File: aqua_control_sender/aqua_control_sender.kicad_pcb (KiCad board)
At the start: 2 copper layers, 66 x 80 mm, 37 parts, among them J1 USB_C, J4 Conn_01x03, J5 Conn_01x03, Q2 IRLML6402, SW1 RESET, SW2 BOOT, U1 ESP32-S3-WROOM-1, U2 LM1117-3.3, U3 RA-02_LORA

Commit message: routing completed
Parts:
- removed Q2: IRLML6402, Package_TO_SOT_SMD:SOT-23
- added J10: ~, Library:TP4056, F.Cu at (65.1, 59.8)
- R8: moved to B.Cu
- moved C7 96.0 mm to (33.9, 92.8), turned to -90 degrees
- moved C6 92.8 mm to (36.1, 92.8), turned to -90 degrees
- moved R17 91.1 mm to (36.1, 96.8)
- moved C5 76.1 mm to (46.1, 72.7), turned to 180 degrees
- moved C4 75.3 mm to (46.1, 74.9), turned to 180 degrees
- moved C9 74.8 mm to (40.4, 62.3), turned to 180 degrees
- moved J8 74.2 mm to (80.7, 92.8)
- moved C8 74.0 mm to (40.4, 65.0), turned to 180 degrees
- moved D4 63.2 mm to (65.2, 50.4), turned to 180 degrees
- moved D3 61.5 mm to (65.2, 53.0), turned to 180 degrees
- moved SW2 53.8 mm to (60.6, 33.4), turned to 180 degrees
- moved R5 51.7 mm to (47.1, 63.2), turned to -90 degrees
- moved TP3 44.3 mm to (60.8, 105.0), turned to 0 degrees
- moved J5 43.8 mm to (41.2, 27.1)
- moved R8 43.2 mm to (60.7, 56.2), turned to 180 degrees
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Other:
- board size 66 x 80 mm -> 54 x 86 mm

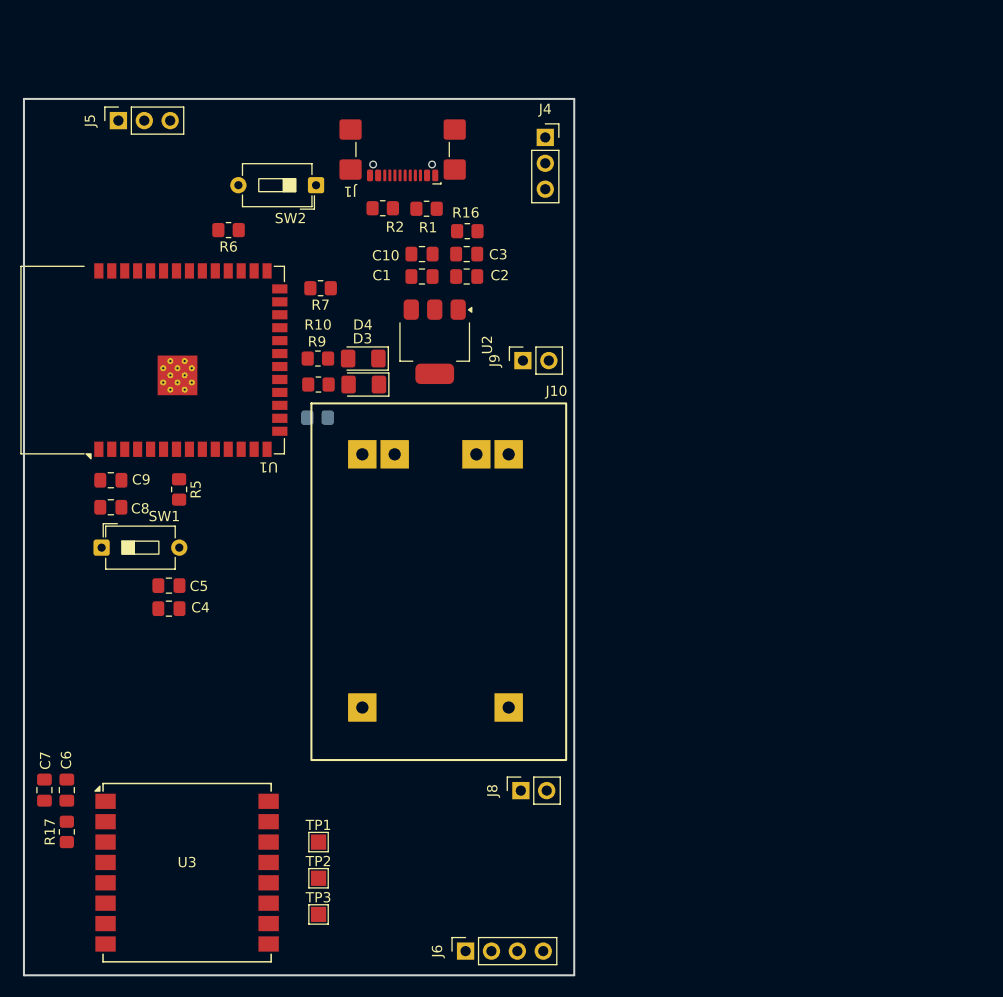
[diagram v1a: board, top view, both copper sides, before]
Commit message: completed routing and added logo
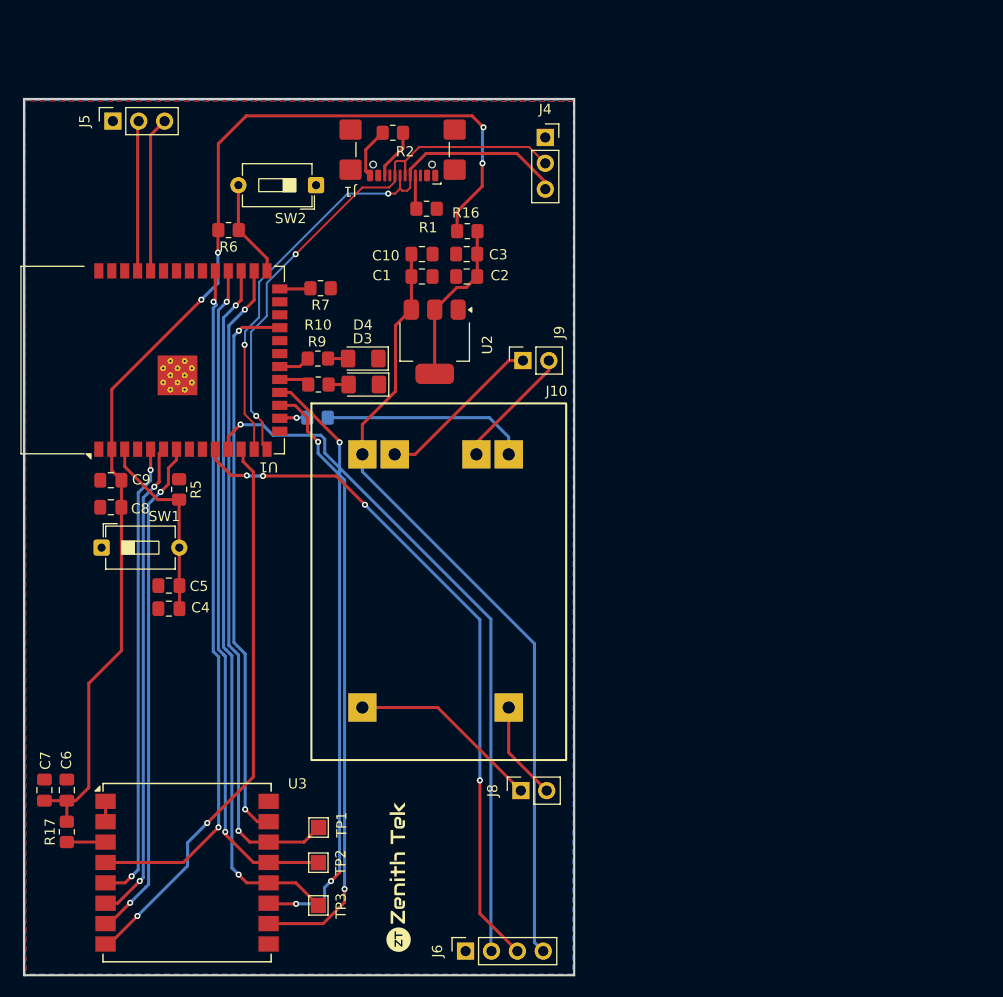
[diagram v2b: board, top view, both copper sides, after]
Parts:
- added G***: LOGO, LOGO, F.Cu at (68.7, 101.3)
- added G***: LOGO, LOGO, B.Cu at (58.7, 76.1)
- moved R2 7.47 mm to (68.1, 28.2)
- moved TP2 1.53 mm to (60.8, 99.9), turned to -90 degrees
- moved TP1 1.43 mm to (60.8, 96.4), turned to -90 degrees
- moved TP3 0.89 mm to (60.8, 104.1), turned to -90 degrees
- moved J5 0.55 mm to (40.6, 27.1)
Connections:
- J4 pad 2: D- -> D+
- J4 pad 3: D+ -> D-
- J5 pad 2: RX -> TX
- J5 pad 3: TX -> RX
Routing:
- net 3.3v: track 0.00 -> 115.1 mm, vias 0 -> 4
- net VCC_3V8: track 0.00 -> 77.7 mm
- net SCK: track 0.00 -> 69.7 mm, vias 0 -> 2
- net TX_ECHO: track 0.00 -> 68.8 mm, vias 0 -> 1
- net RST: track 0.00 -> 67.9 mm, vias 0 -> 2
- net RX_TRIG: track 0.00 -> 67.5 mm, vias 0 -> 4
- net MISO: track 0.00 -> 66.3 mm, vias 0 -> 2
- net MOSI: track 0.00 -> 65.3 mm, vias 0 -> 2
- net DIO4: track 0.00 -> 60.6 mm, vias 0 -> 2
- net DIO5: track 0.00 -> 59.0 mm, vias 0 -> 3
- net DIO3: track 0.00 -> 55.3 mm, vias 0 -> 2
- net D+: track 0.00 -> 55.1 mm, vias 0 -> 2
- net D-: track 0.00 -> 55.1 mm, vias 0 -> 2
- net NSS: track 0.00 -> 54.6 mm, vias 0 -> 2
- net DIO2: track 0.00 -> 49.7 mm, vias 0 -> 2
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- added copper zone on B.Cu, net GND
- added copper zone on F.Cu, net GND

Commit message: sender board complete
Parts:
- removed C4, C9: 100nf, Capacitor_SMD:C_0805_2012Metric_Pad1.18x1.45mm_HandSolder
- removed C5: 1uf, Capacitor_SMD:C_0805_2012Metric_Pad1.18x1.45mm_HandSolder
- removed C8: 47nf, Capacitor_SMD:C_0805_2012Metric_Pad1.18x1.45mm_HandSolder
- removed D3, D4: LED, LED_SMD:LED_1206_3216Metric_Pad1.42x1.75mm_HandSolder
- removed J1: USB_C, Connector_USB:USB_C_Receptacle_GCT_USB4110
- removed J4, J5: Conn_01x03, Connector_PinSocket_2.54mm:PinSocket_1x03_P2.54mm_Vertical
- removed R1, R2: 5.1k, Resistor_SMD:R_0805_2012Metric_Pad1.20x1.40mm_HandSolder
- removed R10, R9: 470E, Resistor_SMD:R_0805_2012Metric_Pad1.20x1.40mm_HandSolder
- removed R5, R6, R7, R8: 10k, Resistor_SMD:R_0805_2012Metric_Pad1.20x1.40mm_HandSolder
- removed SW1: RESET, Button_Switch_THT:SW_DIP_SPSTx01_Slide_6.7x4.1mm_W7.62mm_P2.54mm_LowProfile
- removed SW2: BOOT, Button_Switch_THT:SW_DIP_SPSTx01_Slide_6.7x4.1mm_W7.62mm_P2.54mm_LowProfile
- removed U1: ESP32-S3-WROOM-1, RF_Module:ESP32-S3-WROOM-1
- removed U2: LM1117-3.3, Package_TO_SOT_SMD:SOT-223-3_TabPin2
- added C11: 100nf, Capacitor_SMD:C_0805_2012Metric_Pad1.18x1.45mm_HandSolder, F.Cu at (33.6, 98.4)
- added C12: 47nf, Capacitor_SMD:C_0805_2012Metric_Pad1.18x1.45mm_HandSolder, F.Cu at (36.4, 98.4)
- added D1: 1N5819WS, Diode_SMD:D_SOD-323, F.Cu at (71.7, 38.8)
- added Q1: AO3401A, mosfet:SOT23-3, F.Cu at (34.8, 62.6)
- added Q2: AO3401A, mosfet:SOT23-3, F.Cu at (80.0, 97.4)
- added R11: 100k, Resistor_SMD:R_0805_2012Metric_Pad1.20x1.40mm_HandSolder, F.Cu at (79.0, 82.4)
- added R12: 100k, Resistor_SMD:R_0805_2012Metric_Pad1.20x1.40mm_HandSolder, F.Cu at (80.1, 86.8)
- added R13: 1k, Resistor_SMD:R_0805_2012Metric_Pad1.20x1.40mm_HandSolder, F.Cu at (33.9, 72.8)
- added R14: 1k, Resistor_SMD:R_0805_2012Metric_Pad1.20x1.40mm_HandSolder, F.Cu at (73.9, 98.5)
- added R15: 100k, Resistor_SMD:R_0805_2012Metric_Pad1.20x1.40mm_HandSolder, B.Cu at (79.1, 60.2)
- added R18: 100k, Resistor_SMD:R_0805_2012Metric_Pad1.20x1.40mm_HandSolder, B.Cu at (66.8, 60.2)
- added U4: ESP32-C3_SUPERMINI_TH, esp32c3:MODULE_ESP32-C3_SUPERMINI_TH, F.Cu at (47.5, 92.4)
- added U5: MCP1700x-120xxMB, Package_TO_SOT_SMD:SOT-89-3, F.Cu at (72.5, 83.1)
- moved TP3 68.6 mm to (38.9, 39.1), turned to 0 degrees
- moved TP2 63.1 mm to (43.9, 39.1), turned to 0 degrees
- moved TP1 58.3 mm to (49.5, 39.2), turned to 0 degrees
- moved R16 57.3 mm to (69.2, 94.8), turned to 90 degrees
- moved J8 56.3 mm to (64.9, 38.7), turned to -90 degrees
- moved C3 51.5 mm to (70.2, 91.4), turned to 0 degrees
- moved C10 51.4 mm to (74.6, 91.4), turned to 180 degrees
- moved C2 46.8 mm to (70.2, 88.8), turned to 0 degrees
- moved C1 46.6 mm to (74.6, 88.8), turned to 180 degrees
- moved C7 46.6 mm to (33.5, 46.2)
- moved U3 46.6 mm to (47.5, 54.3)
- moved C6 46.6 mm to (36.0, 46.2)
- moved R17 45.5 mm to (35.8, 51.3), turned to 180 degrees
- moved G*** 37.4 mm to (45.7, 71.8)
- moved J9 34.4 mm to (64.7, 80.9), turned to -90 degrees
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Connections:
- C1 pad 1: VCC_3V8 -> VBAT
- C10 pad 1: VCC_3V8 -> VBAT
- C6 pad 2: 3.3v -> LORA_OUT
- C7 pad 2: 3.3v -> LORA_OUT
- J10 pad 1: VCC_3V8 -> VBAT
- J10 pad 3: BAT- -> GND
- J10 pad 5: SOL_IN+ -> SOL_PWR+
- J6 pad 4: VCC_3V8 -> JSN_OUT
- J9 pad 2: BAT- -> GND
- R17 pad 2: 3.3v -> LORA_OUT
- U3 pad 10: DIO4 -> unconnected-(U3-DI04-Pad10)
- U3 pad 11: DIO5 -> unconnected-(U3-DI05-Pad11)
- U3 pad 6: DIO1 -> unconnected-(U3-DI01-Pad6)
- U3 pad 7: DIO2 -> unconnected-(U3-DI02-Pad7)
- U3 pad 8: DIO3 -> unconnected-(U3-DI03-Pad8)
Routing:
- net VCC_3V8: track 77.7 -> 0.00 mm
- net DIO4: track 60.6 -> 0.00 mm, vias 2 -> 0
- net DIO5: track 59.0 -> 0.00 mm, vias 3 -> 0
- net DIO3: track 55.3 -> 0.00 mm, vias 2 -> 0
- net D+: track 55.1 -> 0.00 mm, vias 2 -> 0
- net D-: track 55.1 -> 0.00 mm, vias 2 -> 0
- net SOL_IN: track 0.00 -> 54.6 mm, vias 0 -> 1
- net DIO2: track 49.7 -> 0.00 mm, vias 2 -> 0
- net DIO1: track 47.6 -> 0.00 mm, vias 2 -> 0
- net BAT_IN: track 0.00 -> 46.6 mm, vias 0 -> 2
- net LORA_PWR: track 0.00 -> 43.0 mm, vias 0 -> 3
- net VBAT: track 0.00 -> 41.9 mm
- net 3.3v: track 115.1 -> 80.6 mm, vias 4 -> 1
- net TX_ECHO: track 68.8 -> 36.1 mm
- net JSN_PWR: track 0.00 -> 30.8 mm, vias 0 -> 2
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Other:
- board size 54 x 86 mm -> 54 x 75.4 mm
- board text added: "AquaControl_Sender v2.1.0"
- board text added: "C6"

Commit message: final version
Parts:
- renumbered TP2 to MISO, TP1 to MOSI, TP3 to SCK
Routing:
- net SCK: track 77.7 -> 78.6 mm
- net MISO: track 79.0 -> 79.9 mm
- net JSN_PWR: track 30.8 -> 30.0 mm, vias 2 -> 1
